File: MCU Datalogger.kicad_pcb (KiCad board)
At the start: 2 copper layers, 52.1 x 31.8 mm, 30 parts, among them J1 Conn_01x04_Pin, J2 Conn_01x09_Pin, J3 Conn_01x04_Pin, J4 Conn_02x03_Odd_Even, U1 DS1337S_, U2 24LC1025, U3 24LC1025, U4 ATMEGA328P-AU, Y1 32.768 KHz, Y2 16 MHz

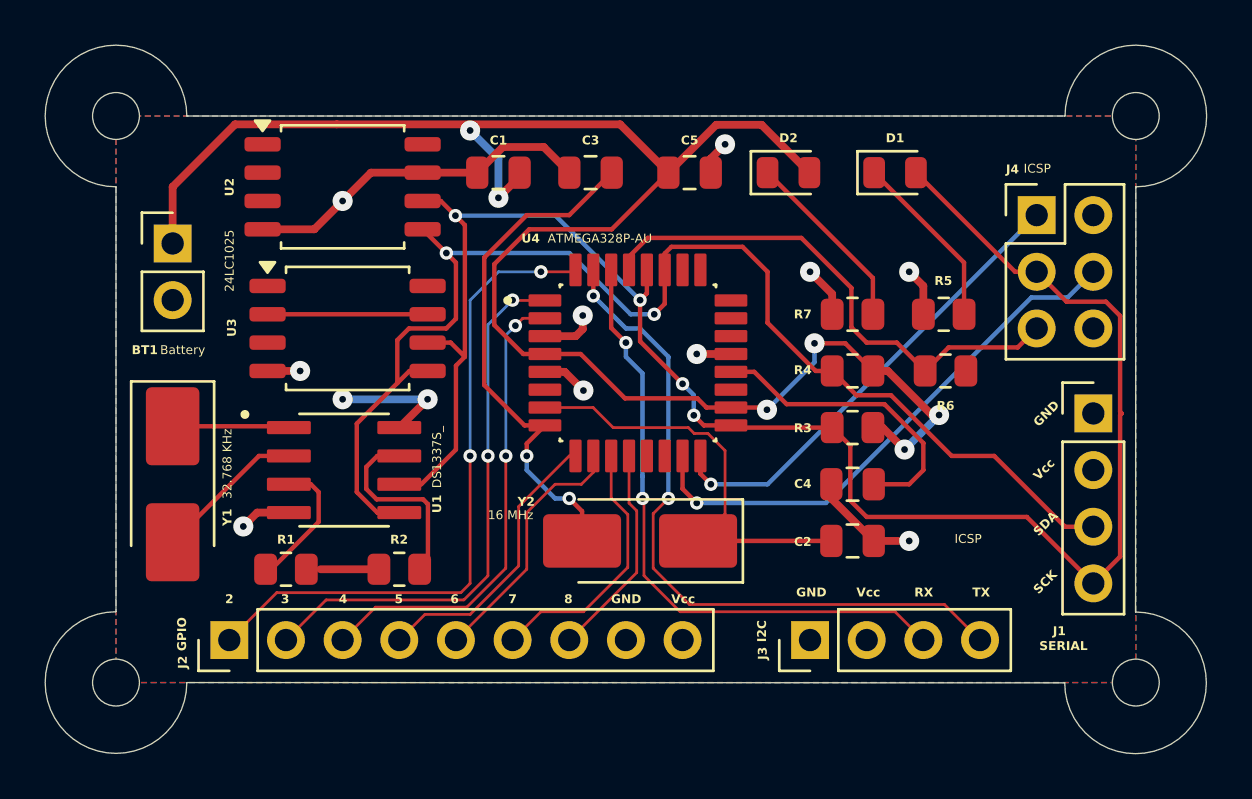
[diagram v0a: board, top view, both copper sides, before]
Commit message: Rename project folder to remove space
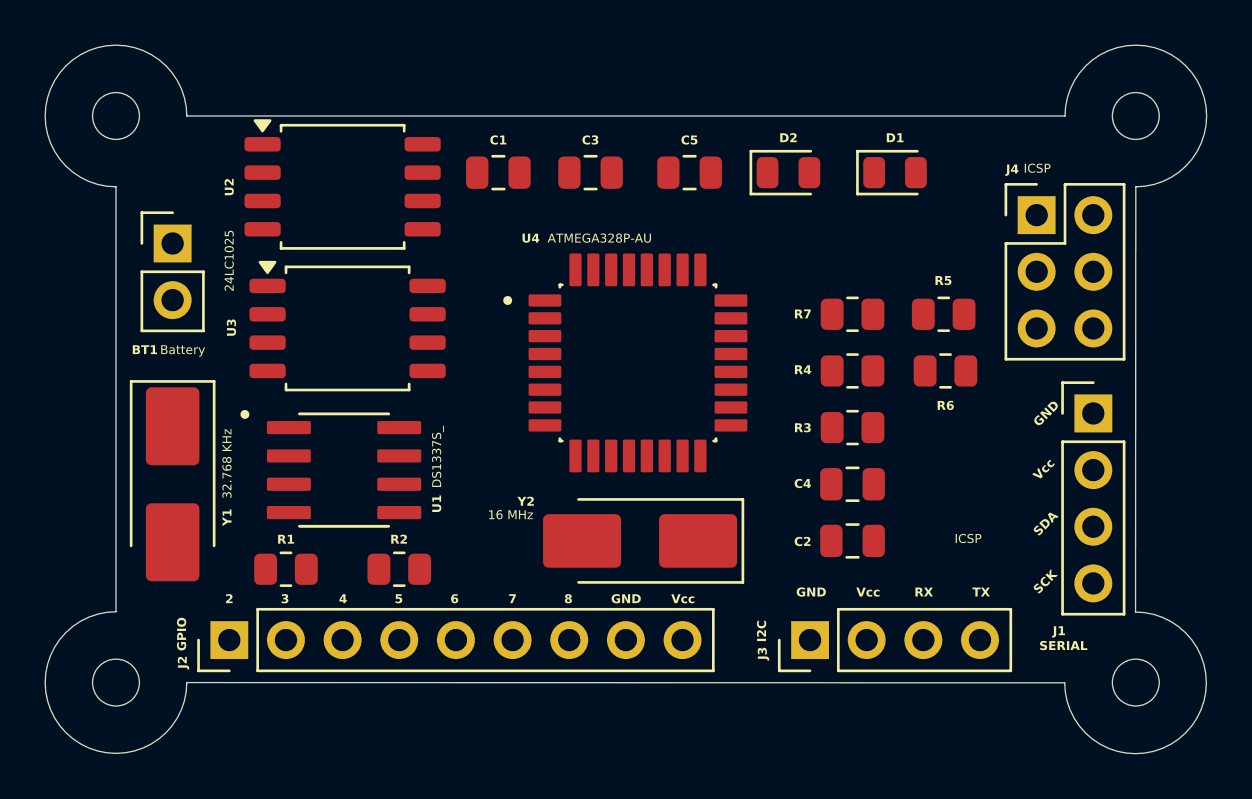
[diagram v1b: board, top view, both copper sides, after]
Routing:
- net /Vcc: track 88.7 -> 0.00 mm, vias 8 -> 0
- net /SCK: track 82.0 -> 0.00 mm, vias 4 -> 0
- net /SDA: track 58.3 -> 0.00 mm, vias 2 -> 0
- net GND: track 36.5 -> 0.00 mm, vias 10 -> 0
- net /TX: track 31.4 -> 0.00 mm, vias 2 -> 0
- net /D2: track 29.8 -> 0.00 mm, vias 2 -> 0
- net /RX: track 28.0 -> 0.00 mm, vias 2 -> 0
- net /D3: track 24.5 -> 0.00 mm, vias 2 -> 0
- net /MOSI: track 24.4 -> 0.00 mm, vias 1 -> 0
- net /RESET: track 23.5 -> 0.00 mm
- net Net-(U4-PB7): track 23.4 -> 0.00 mm, vias 2 -> 0
- net /D4: track 21.2 -> 0.00 mm, vias 2 -> 0
- net /MISO: track 21.1 -> 0.00 mm, vias 1 -> 0
- net Net-(U4-PB6): track 19.4 -> 0.00 mm
- net Net-(U4-AREF): track 13.6 -> 0.00 mm
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- removed copper zone on F.Cu, net /Vcc
- removed copper zone on B.Cu, net GND
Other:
- copper layers 2 -> 4
